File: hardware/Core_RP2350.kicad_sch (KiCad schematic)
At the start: 67 parts, among them U1 RP2350B-QFN80, U2 LM4040A30IDBZR, U3 W25Q128JVS, U4 W25Q128JVS, U5 W25Q128JVS

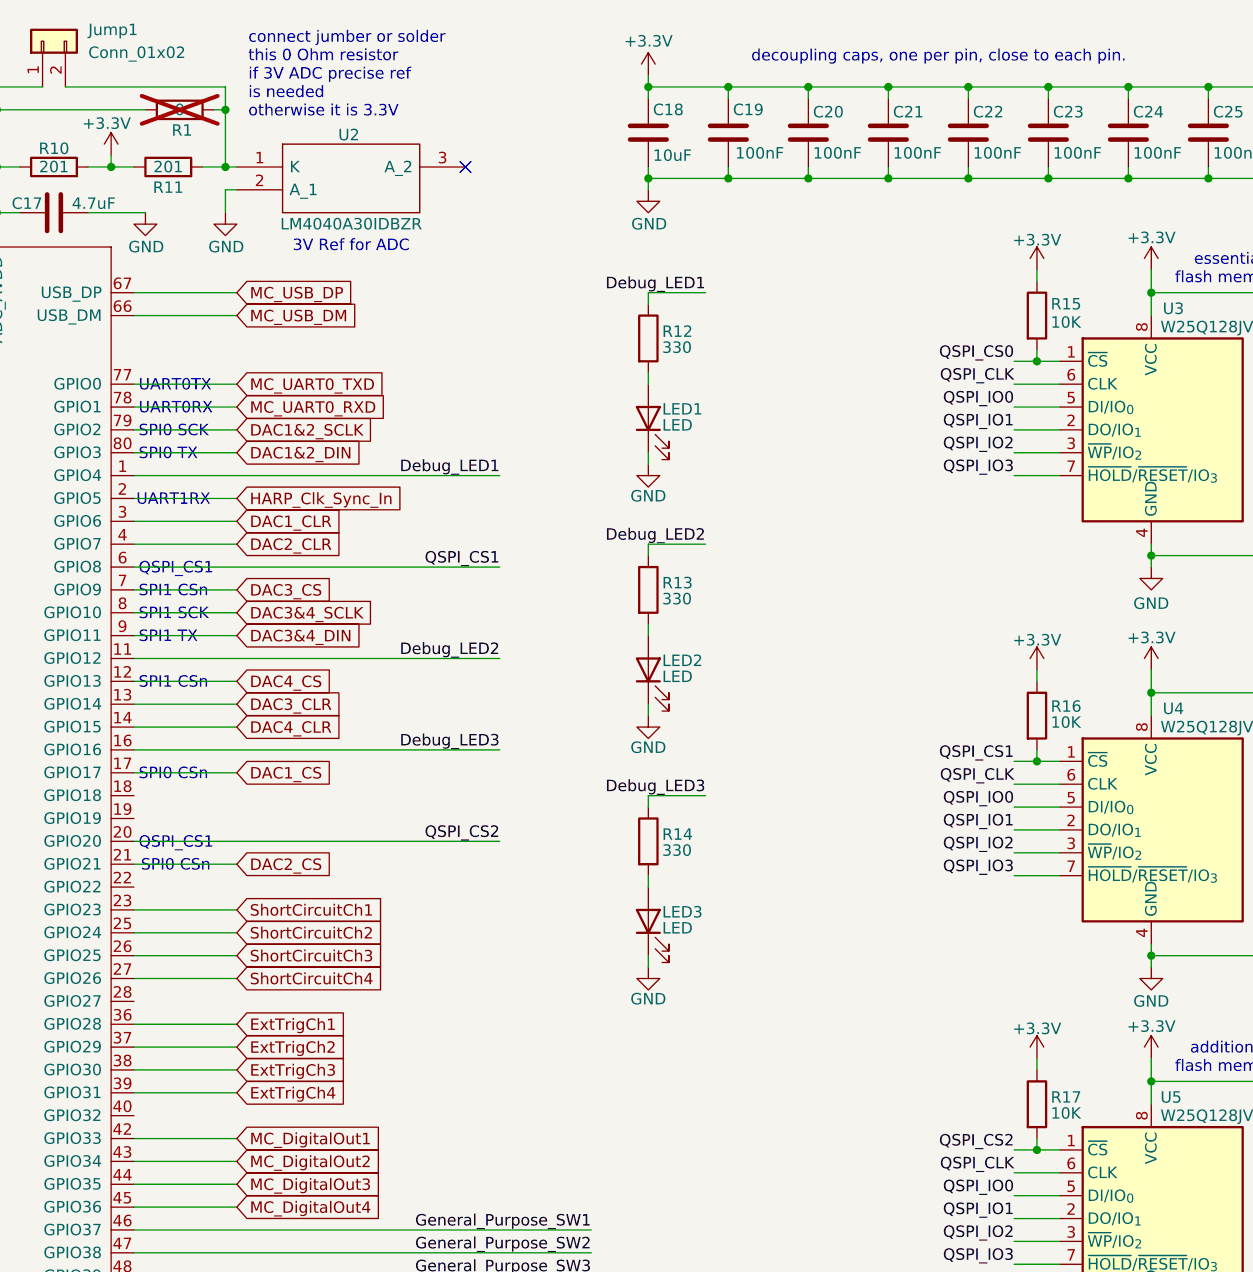
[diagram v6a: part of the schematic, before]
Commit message: The part designators have been reannotated.
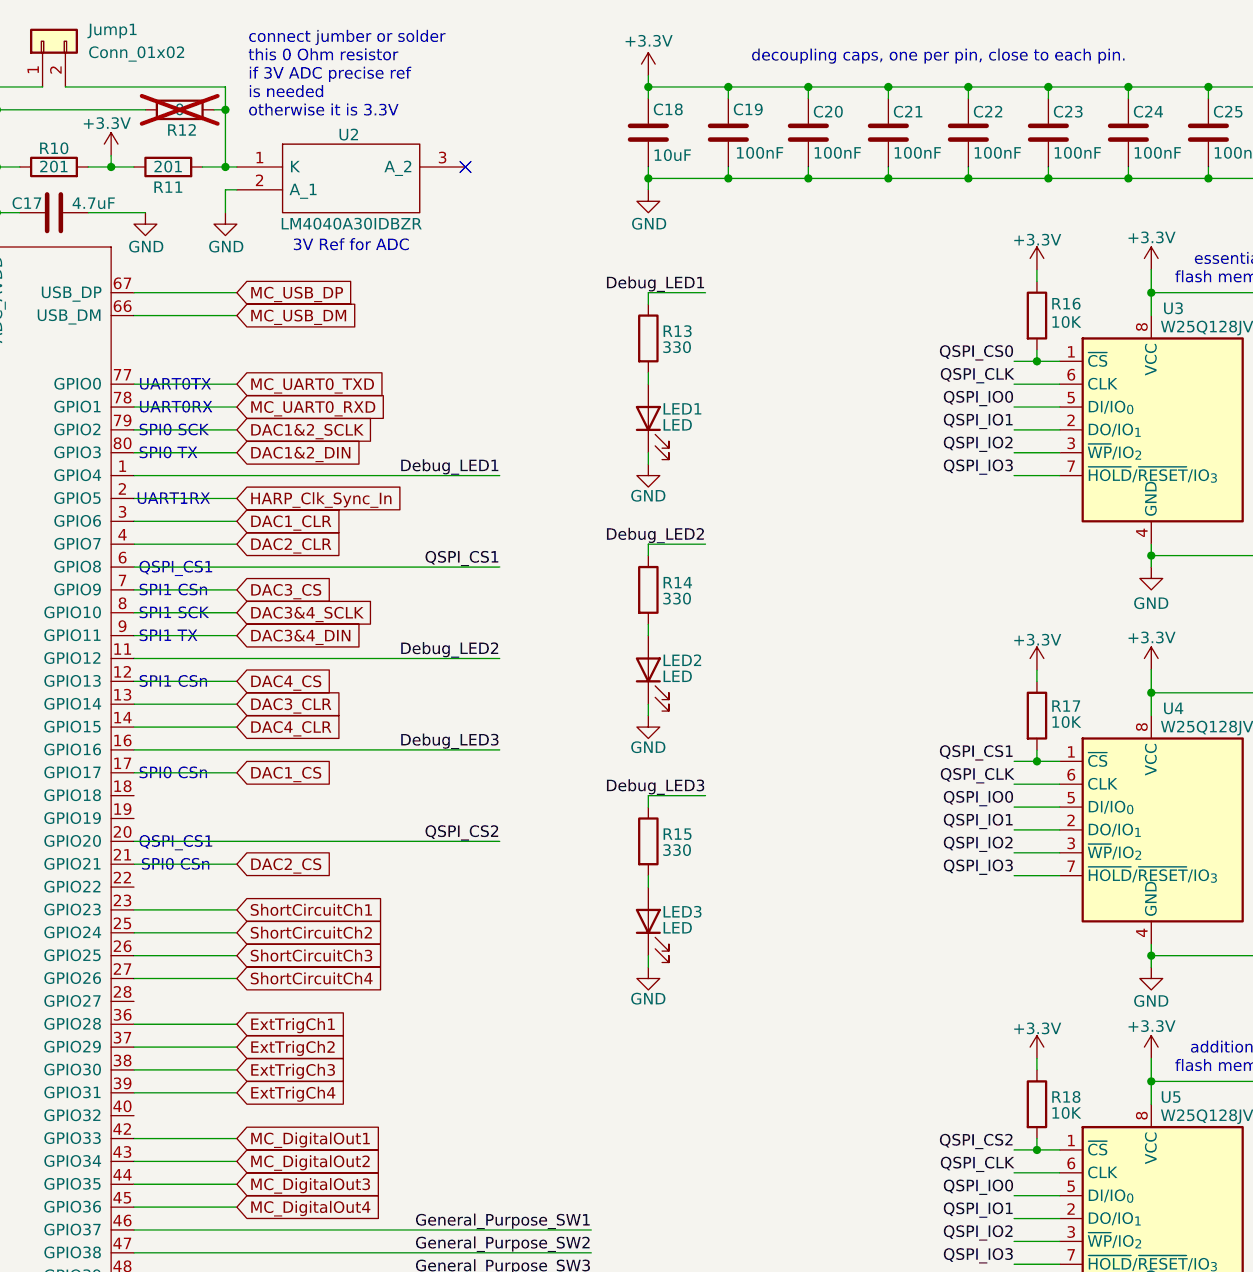
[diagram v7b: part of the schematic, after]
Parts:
- renumbered R1 to R12, R12 to R13, R13 to R14, R14 to R15, R15 to R16, R16 to R17, R17 to R18
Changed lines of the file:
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@@
 		(on_board yes)
 		(dnp no)
-		(property "Reference" "R13"
+		(property "Reference" "R14"
 			(at 208.534 74.168 0)
 			(effects
@@
 			(project "harp.device.quad.dac"
 				(path "/6b47c519-21c4-43bd-9777-b273999e4447/5973743b-c3fc-4963-acef-26c8fa426708"
-					(reference "R13")
+					(reference "R14")
 					(unit 1)
 				)
@@
 		(on_board yes)
 		(dnp no)
-		(property "Reference" "R14"
+		(property "Reference" "R15"
 			(at 208.534 102.108 0)
 			(effects
@@
 			(project "harp.device.quad.dac"
 				(path "/6b47c519-21c4-43bd-9777-b273999e4447/5973743b-c3fc-4963-acef-26c8fa426708"
-					(reference "R14")
+					(reference "R15")
 					(unit 1)
 				)
@@
 		(on_board yes)
 		(dnp no)
-		(property "Reference" "R12"
+		(property "Reference" "R13"
 			(at 208.534 46.228 0)
 			(effects
@@
 			(project "harp.device.quad.dac"
 				(path "/6b47c519-21c4-43bd-9777-b273999e4447/5973743b-c3fc-4963-acef-26c8fa426708"
-					(reference "R12")
+					(reference "R13")
 					(unit 1)
 				)
@@
 		(on_board yes)
 		(dnp no)
-		(property "Reference" "R16"
+		(property "Reference" "R17"
 			(at 251.714 87.884 0)
 			(effects
@@
 			(project "harp.device.quad.dac"
 				(path "/6b47c519-21c4-43bd-9777-b273999e4447/5973743b-c3fc-4963-acef-26c8fa426708"
-					(reference "R16")
+					(reference "R17")
 					(unit 1)
 				)
@@
 		(on_board yes)
 		(dnp no)
-		(property "Reference" "R15"
+		(property "Reference" "R16"
 			(at 251.714 43.18 0)
 			(effects
@@
 			(project "harp.device.quad.dac"
 				(path "/6b47c519-21c4-43bd-9777-b273999e4447/5973743b-c3fc-4963-acef-26c8fa426708"
-					(reference "R15")
+					(reference "R16")
 					(unit 1)
 				)
@@
 		(on_board no)
 		(dnp yes)
-		(property "Reference" "R1"
+		(property "Reference" "R12"
 			(at 155.194 23.876 90)
 			(effects
@@
 			(project "harp.device.quad.dac"
 				(path "/6b47c519-21c4-43bd-9777-b273999e4447/5973743b-c3fc-4963-acef-26c8fa426708"
-					(reference "R1")
+					(reference "R12")
 					(unit 1)
 				)
@@
 		(on_board yes)
 		(dnp no)
-		(property "Reference" "R17"
+		(property "Reference" "R18"
 			(at 251.714 131.318 0)
 			(effects
@@
 			(project "harp.device.quad.dac"
 				(path "/6b47c519-21c4-43bd-9777-b273999e4447/5973743b-c3fc-4963-acef-26c8fa426708"
-					(reference "R17")
+					(reference "R18")
 					(unit 1)
 				)

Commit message: Some improvements have been made to the layout.
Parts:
- removed FID4: Fiducial, harp.device.quad.dac.kicad:Fiducial_0.5mm_Mask1mm, symbol harp.device.quad.dac:Fiducial
- added H1, H2, H3, H4: MountingHole_Pad, harp.device.quad.dac.kicad:MountingHole_3.2mm_M3_DIN965, symbol harp.device.quad.dac:MountingHole_Pad
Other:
- note added: "QSPI_CS2"
